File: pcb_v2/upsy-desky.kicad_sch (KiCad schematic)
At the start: 39 parts, among them J1 RJ45, J2 RJ45, J3 USB_C_ReceptacleUSB2.0, Q1 MMBT3904, Q2 MMBT3904, Q3 2N7002, Q4 2N7002, Q5 2N7002, Q6 2N7002, Q7 2N7002, Q8 2N7002, U2 AMS1117-3.3, U3 ESP32-WROOM-32

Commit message: Modify the schematics
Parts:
- removed D2: LED, LED_SMD:LED_0603_1608Metric, symbol Device:LED
- removed Q1, Q2: MMBT3904, Package_TO_SOT_SMD:SOT-23, symbol Transistor_BJT:MMBT3904
- removed R22: 940, Resistor_SMD:R_0402_1005Metric, symbol Device:R
- removed U3: ESP32-WROOM-32, RF_Module:ESP32-WROOM-32, symbol RF_Module:ESP32-WROOM-32
- added C6, C7: 15p, Capacitor_SMD:C_0402_1005Metric, symbol Device:C
- added C8: 4.7u, Capacitor_SMD:C_0402_1005Metric, symbol Device:C
- added C9: 100n, Capacitor_SMD:C_0402_1005Metric, symbol Device:C
- added H1, H2, H3: MountingHole, MountingHole:MountingHole_2.2mm_M2_Pad, symbol Mechanical:MountingHole
- added J4: Conn_01x03_Socket, Connector:FanPinHeader_1x03_P2.54mm_Vertical, symbol Connector:Conn_01x03_Socket
- added J5: Screw_Terminal_01x03, TerminalBlock:TerminalBlock_Altech_AK300-3_P5.00mm, symbol Connector:Screw_Terminal_01x03
- added J6: Conn_01x03_Pin, Connector_JST:JST_EH_B3B-EH-A_1x03_P2.50mm_Vertical, symbol Connector:Conn_01x03_Pin
- added R18: 0, Resistor_SMD:R_0402_1005Metric, symbol Device:R
- added R19, R20: 10k, Resistor_SMD:R_0402_1005Metric, symbol Device:R
- added SW1: SW_Push, Button_Switch_SMD:SW_Push_1P1T_NO_CK_KMR2, symbol Switch:SW_Push
- added TP1, TP10, TP11, TP2, TP3, TP4, TP5, TP6, TP7, TP8, TP9: TestPoint, TestPoint:TestPoint_Pad_D1.0mm, symbol Connector:TestPoint
- added U1: VL53L0CXV0DH1, Sensor_Distance:ST_VL53L1x, symbol Sensor_Distance:VL53L0CXV0DH1
- added U4: ESP32-C3-WROOM-02, PCM_Espressif:ESP32-C3-WROOM-02, symbol PCM_Espressif:ESP32-C3-WROOM-02
- added Y1: 32K, Crystal:Crystal_SMD_2012-2Pin_2.0x1.2mm, symbol Device:Crystal
- J1, J2: footprint footprints:ASSMANN_A-2004-2-4-LPS-N-R -> Connector_RJ:RJ45_Amphenol_54602-x08_Horizontal
- R21: value 470 -> 0; Checked Y -> (none); Comment Any 5V or higher rated resistor will work fine -> (none); LCSC C25117 -> (none); MPN RC1005J471CS -> (none); Package 0402 -> (none); now not fitted
- R3, R4: value 10k -> 2k2; Checked Y -> (none); Comment Any 5V or higher rated resistor will work fine -> (none); LCSC C25744 -> (none); MPN RC0402JR-1310KL -> (none); Package 0402 -> (none)
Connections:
- net DTR is gone; now on net +3V3: R4.1
- net RTS is gone; now on net +3V3: R3.1
- net +3V3: now also C8.1, C9.1, R19.1, R20.1, U1.1 (AVDDVCSEL), U1.11 (AVDD), U4.1 (3V3)
- net EN: now also SW1.2, TP7.1, U4.2 (EN/CHIP_PU)
- net GND: now also C6.2, C7.2, C8.2, C9.2, J5.1 (Pin_1), J6.3 (Pin_3), SW1.1, U1.12 (GND), U1.2 (AVSSVCSEL), U1.3 (GND), U1.4 (GND), U1.6 (GND), U4.19 (GND), U4.9 (GND)
- net GPIO0: now also C6.1, R18.2, U4.18 (GPIO0/ADC1_CH0/XTAL_32K_P), Y1.2
- net USB_CC1: now also TP2.1
- net USB_CC2: now also TP1.1
- net VBUS: now also J4.3 (Pin_3), J5.3 (Pin_3), TP5.1; no longer D1.2 (A)
- net SCL: now reaches R3.2
- net SCL: now also TP10.1, U1.10 (SCL), U4.3 (GPIO4/ADC1_CH4)
- net GPIO1: now reaches R21.2
- net GPIO1: now also C7.1, U4.17 (GPIO1/ADC1_CH1/XTAL_32K_N), Y1.1
- net SDA: now reaches R4.2
- net SDA: now also TP11.1, U1.9 (SDA), U4.4 (GPIO5/ADC2_CH0)
- net +5V renamed VDD
- net VDD: now also J4.1 (Pin_1), TP3.1; no longer C1.1, D1.1 (K), U2.3 (VI)
- net GPIO16 renamed GPIO9
- net GPIO9: now also U4.8 (GPIO9)
- net GPIO17 renamed GPIO8
- net GPIO8: now also U4.7 (GPIO8)
- net GPIO18 renamed GPIO7
- net GPIO7: now also U4.6 (GPIO7)
- net GPIO19 renamed GPIO2
- net GPIO2: now also U4.16 (GPIO2/ADC1_CH2)
- net GPIO21 renamed GPIO10
- net GPIO10: now also U4.10 (GPIO10)
- net GPIO22 renamed GPIO3
- net GPIO3: now also U4.15 (GPIO3/ADC1_CH3)
- net GPIO23: no longer names the net of R21.1
- net GPIO23: now also R19.2, U1.5 (XSHUT)
- net USB_D+ renamed USB_DP
- net USB_DP: now also U4.14 (GPIO19/USB_D+)
- net USB_D- renamed USB_DN
- net USB_DN: now also U4.13 (GPIO18/USB_D-)
- new net: C1.1, D1.1 (K), U2.3 (VI)
- new net: D1.2 (A), J4.2 (Pin_2), TP4.1
- new net DBG_RX: J6.1 (Pin_1), TP8.1, U4.11 (GPIO20/U0RXD)
- new net DBG_TX: J6.2 (Pin_2), TP9.1, U4.12 (GPIO21/U0TXD)
- new net INT: R18.1, R20.2, U1.7 (GPIO1)
- new net LED_RGB: J5.2 (Pin_2), TP6.1, U4.5 (GPIO6)
- no-connect marks 24 -> 2
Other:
- note added: "Debug Serial Port"
- note added: "Distance sensor"
- note added: "ESP32 C3 MCU"
- note added: "ESP32 C3 Power Supply"
- note added: "LED RGB Strip"
- note added: "RJ45 Connectors"
- note added: "USB C Connection"
- note added: "Voltage level shifters"
- company: (none) -> Petr Hodina
- title: Upsy Desky -> (Risky) Upsy Desky
- moved on the sheet: C1, C2, C3, C4, C5, D1, J1, J2, Q3, Q4, Q5, Q6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

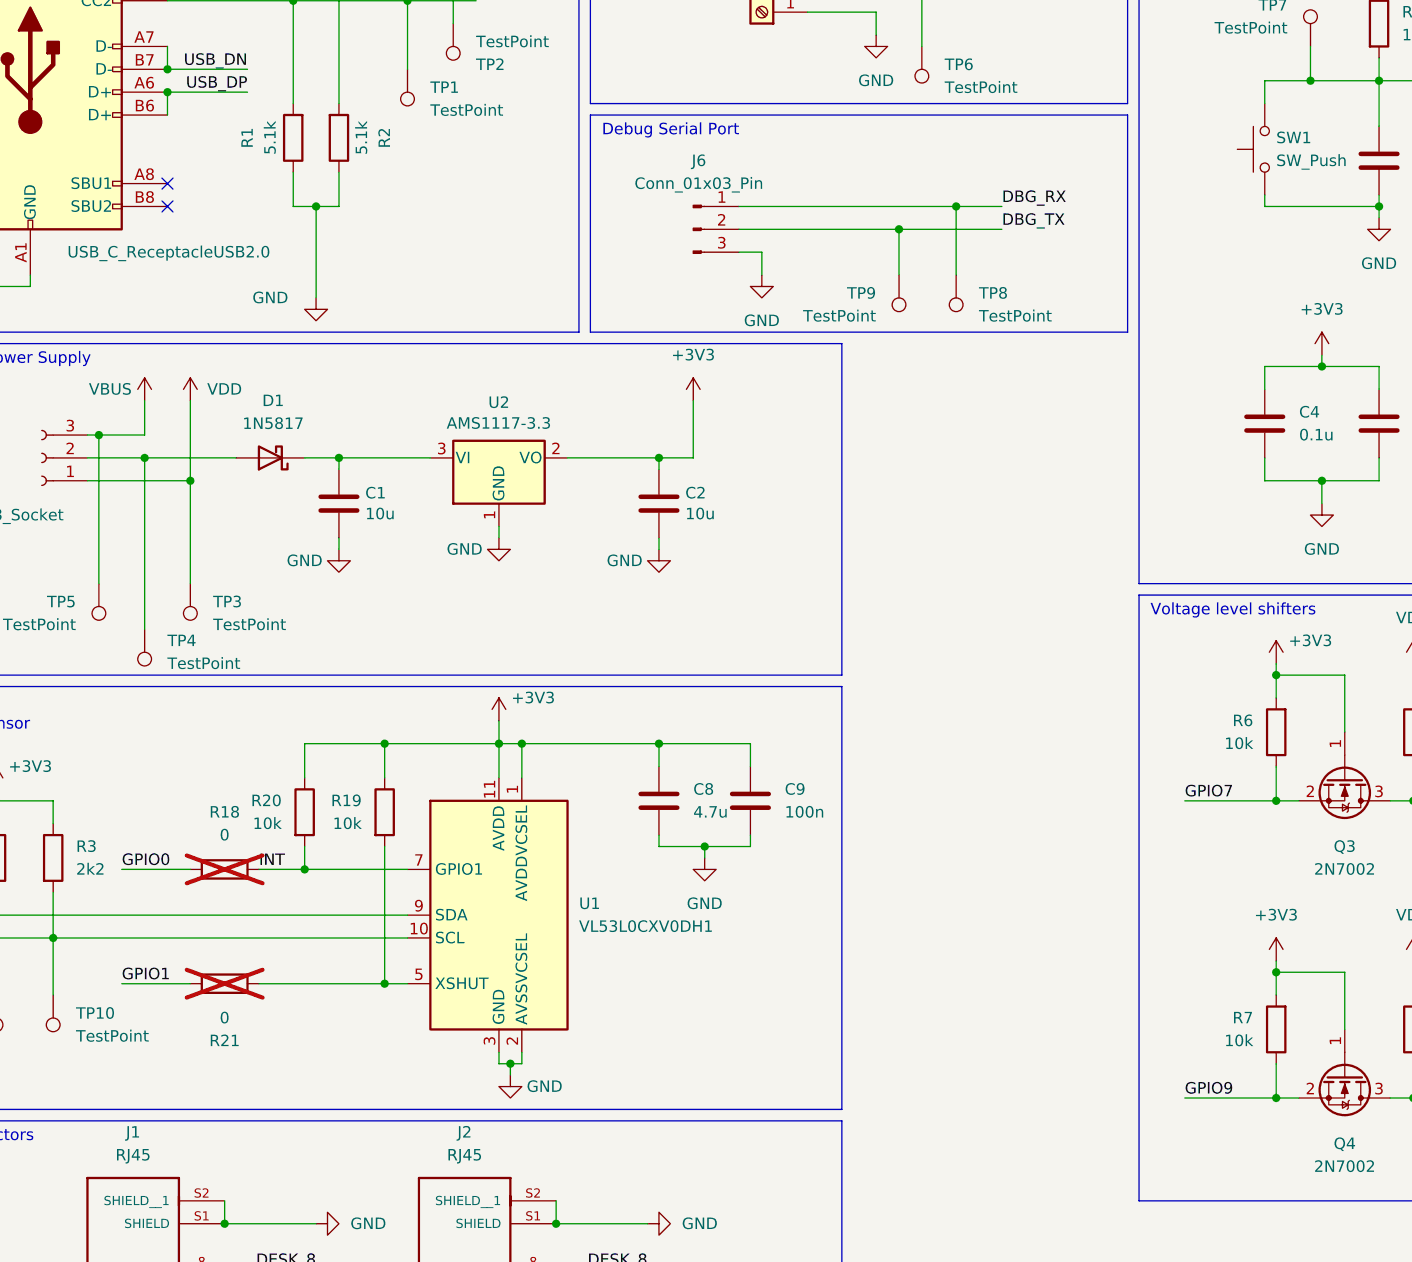
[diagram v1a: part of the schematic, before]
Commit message: Several improvements:
- Improved GND connection to the ESP32 module.
- Connected the UART signals to SBU pins.
- Rounded corners
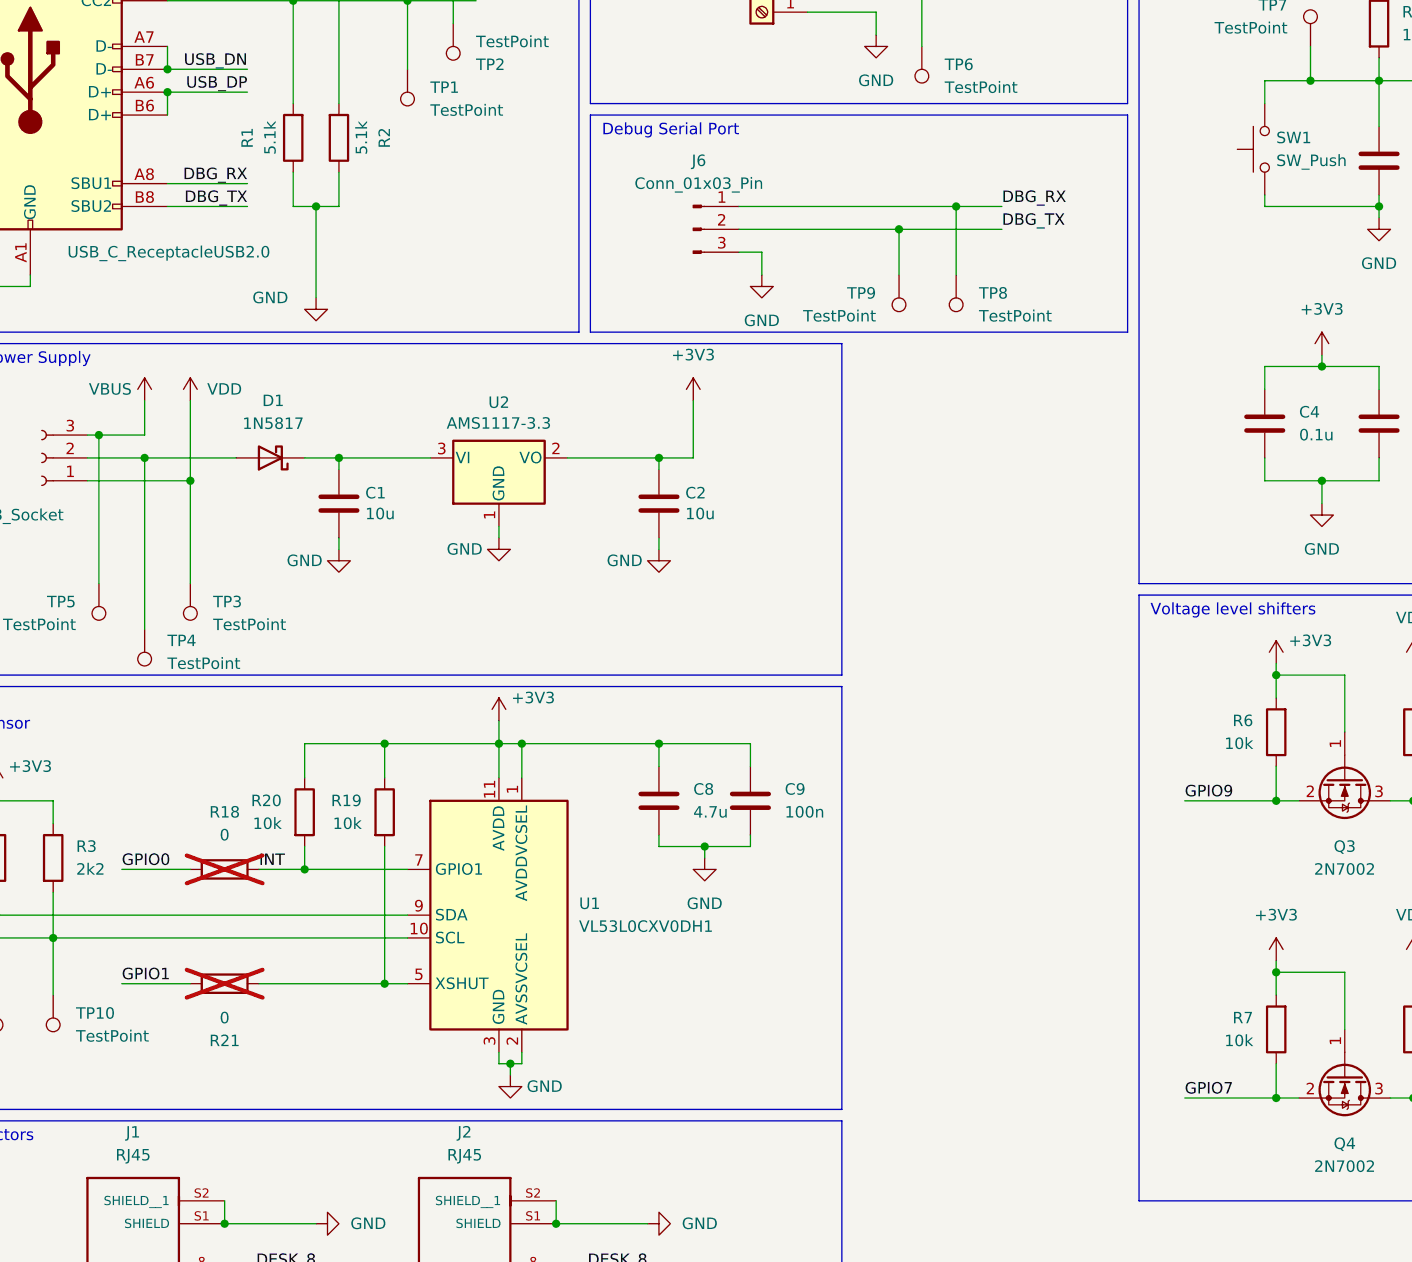
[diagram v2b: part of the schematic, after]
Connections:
- net DBG_RX: now also J3.A8 (SBU1)
- net DBG_TX: now also J3.B8 (SBU2)
- net GPIO7: now also Q4.2 (S), R7.1; no longer Q3.2 (S), R6.1
- net GPIO9: now also Q3.2 (S), R6.1; no longer Q4.2 (S), R7.1
- no-connect marks 2 -> 0
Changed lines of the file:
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@@
   (junction (at 255.27 138.43) (diameter 0) (color 0 0 0 0)
   )
-  (no_connect (at 44.45 50.8))
-  (no_connect (at 44.45 53.34))
   (wire (pts (xy 179.07 71.12) (xy 179.07 73.66))
     (stroke (width 0) (type default))
@@
     (stroke (width 0) (type default))
   )
+  (wire (pts (xy 44.45 53.34) (xy 53.34 53.34))
+    (stroke (width 0) (type default))
+  )
   (wire (pts (xy 242.57 21.59) (xy 242.57 24.13))
     (stroke (width 0) (type default))
@@
     (stroke (width 0) (type default))
   )
+  (wire (pts (xy 44.45 50.8) (xy 53.34 50.8))
+    (stroke (width 0) (type default))
+  )
   (wire (pts (xy 83.82 147.32) (xy 83.82 148.59))
     (stroke (width 0) (type default))
@@
     (effects (font (size 1.27 1.27)) (justify right bottom))
   )
-  (label "GPIO9" (at 157.48 152.4 0) (fields_autoplaced)
+  (label "GPIO7" (at 157.48 152.4 0) (fields_autoplaced)
     (effects (font (size 1.27 1.27)) (justify left bottom))
   )
@@
     (effects (font (size 1.27 1.27)) (justify right bottom))
   )
-  (label "GPIO7" (at 157.48 119.38 0) (fields_autoplaced)
+  (label "GPIO9" (at 157.48 119.38 0) (fields_autoplaced)
     (effects (font (size 1.27 1.27)) (justify left bottom))
   )
@@
     (effects (font (size 1.27 1.27)) (justify right bottom))
   )
+  (label "DBG_TX" (at 53.34 53.34 180) (fields_autoplaced)
+    (effects (font (size 1.27 1.27)) (justify right bottom))
+  )
   (label "EN" (at 184.15 39.37 0) (fields_autoplaced)
     (effects (font (size 1.27 1.27)) (justify left bottom))
@@
     (effects (font (size 1.27 1.27)) (justify right bottom))
   )
+  (label "DBG_RX" (at 53.34 50.8 180) (fields_autoplaced)
+    (effects (font (size 1.27 1.27)) (justify right bottom))
+  )
